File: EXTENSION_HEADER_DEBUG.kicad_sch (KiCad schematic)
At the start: 0 parts

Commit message: Weiter gemacht
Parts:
- added J8: Conn_01x16_MountingPin, Connector_PinHeader_2.54mm:PinHeader_2x08_P2.54mm_Vertical_SMD, symbol Connector_Generic_MountingPin:Conn_01x16_MountingPin
- added J9: Conn_01x04_MountingPin, Connector_PinHeader_2.54mm:PinHeader_1x04_P2.54mm_Vertical_SMD_Pin1Left, symbol Connector_Generic_MountingPin:Conn_01x04_MountingPin
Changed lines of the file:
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@@
 		(rev "Rev 1")
 	)
+	(symbol
+		(lib_id "Connector_Generic_MountingPin:Conn_01x04_MountingPin")
+		(at 66.04 154.94 0)
+		(unit 1)
+		(exclude_from_sim no)
+		(in_bom yes)
+		(on_board yes)
+		(dnp no)
+		(fields_autoplaced yes)
+		(property "Reference" "J9"
+			(at 68.58 155.2955 0)
+			(effects
+				(font
+					(size 1.27 1.27)
+				)
+				(justify left)
+			)
+		)
+		(property "Value" "Conn_01x04_MountingPin"
+			(at 68.58 157.8355 0)
+			(effects
+				(font
+					(size 1.27 1.27)
+				)
+				(justify left)
+			)
+		)
+		(property "Footprint" "Connector_PinHeader_2.54mm:PinHeader_1x04_P2.54mm_Vertical_SMD_Pin1Left"
+			(at 66.04 154.94 0)
+			(effects
+				(font
+					(size 1.27 1.27)
+				)
+				(hide yes)
+			)
+		)
+		(property "Datasheet" "~"
+			(at 66.04 154.94 0)
+			(effects
+				(font
+					(size 1.27 1.27)
+				)
+				(hide yes)
+			)
+		)
+		(property "Description" "Generic connectable mounting pin connector, single row, 01x04, script generated (kicad-library-utils/schlib/autogen/connector/)"
+			(at 66.04 154.94 0)
+			(effects
+				(font
+					(size 1.27 1.27)
+				)
+				(hide yes)
+			)
+		)
+		(pin "MP"
+		)
+		(pin "2"
+		)
+		(pin "3"
+		)
+		(pin "4"
+		)
+		(pin "1"
+		)
+		(instances
+			(project ""
+				(path "/96aa4cdc-6548-43b6-b96a-6d1618c17d83/727687ad-08f4-4d44-9d98-36b0cbf3889d"
+					(reference "J9")
+					(unit 1)
+				)
+			)
+		)
+	)
+	(symbol
+		(lib_id "Connector_Generic_MountingPin:Conn_01x16_MountingPin")
+		(at 67.31 106.68 0)
+		(unit 1)
+		(exclude_from_sim no)
+		(in_bom yes)
+		(on_board yes)
+		(dnp no)
+		(fields_autoplaced yes)
+		(property "Reference" "J8"
+			(at 69.85 107.0355 0)
+			(effects
+				(font
+					(size 1.27 1.27)
+				)
+				(justify left)
+			)
+		)
+		(property "Value" "Conn_01x16_MountingPin"
+			(at 69.85 109.5755 0)
+			(effects
+				(font
+					(size 1.27 1.27)
+				)
+				(justify left)
+			)
+		)
+		(property "Footprint" "Connector_PinHeader_2.54mm:PinHeader_2x08_P2.54mm_Vertical_SMD"
+			(at 67.31 106.68 0)
+			(effects
+				(font
+					(size 1.27 1.27)
+				)
+				(hide yes)
+			)
+		)
+		(property "Datasheet" "~"
+			(at 67.31 106.68 0)
+			(effects
+				(font
+					(size 1.27 1.27)
+				)
+				(hide yes)
+			)
+		)
+		(property "Description" "Generic connectable mounting pin connector, single row, 01x16, script generated (kicad-library-utils/schlib/autogen/connector/)"
+			(at 67.31 106.68 0)
+			(effects
+				(font
+					(size 1.27 1.27)
+				)
+				(hide yes)
+			)
+		)
+		(pin "6"
+		)
+		(pin "14"
+		)
+		(pin "4"
+		)
+		(pin "11"
+		)
+		(pin "1"
+		)
+		(pin "12"
+		)
+		(pin "10"
+		)
+		(pin "13"
+		)
+		(pin "MP"
+		)
+		(pin "2"
+		)
+		(pin "3"
+		)
+		(pin "5"
+		)
+		(pin "7"
+		)
+		(pin "8"
+		)
+		(pin "9"
+		)
+		(pin "15"
+		)
+		(pin "16"
+		)
+		(instances
+			(project ""
+				(path "/96aa4cdc-6548-43b6-b96a-6d1618c17d83/727687ad-08f4-4d44-9d98-36b0cbf3889d"
+					(reference "J8")
+					(unit 1)
+				)
+			)
+		)
+	)
 )

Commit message: Layout + Schematic weiter gemacht
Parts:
- removed J8: Conn_01x16_MountingPin, Connector_PinHeader_2.54mm:PinHeader_2x08_P2.54mm_Vertical_SMD, symbol Connector_Generic_MountingPin:Conn_01x16_MountingPin
- removed J9: Conn_01x04_MountingPin, Connector_PinHeader_2.54mm:PinHeader_1x04_P2.54mm_Vertical_SMD_Pin1Left, symbol Connector_Generic_MountingPin:Conn_01x04_MountingPin
- added H1, H2, H3, H4: MountingHole_Pad_MP, MountingHole:MountingHole_3.2mm_M3_Pad, symbol Mechanical:MountingHole_Pad_MP
- added J8: Conn_01x16_Pin, Connector_PinHeader_2.54mm:PinHeader_2x08_P2.54mm_Vertical_SMD, symbol Connector:Conn_01x16_Pin
- added J9: Conn_01x04_Pin, Connector_PinHeader_2.54mm:PinHeader_1x04_P2.54mm_Vertical_SMD_Pin1Left, symbol Connector:Conn_01x04_Pin
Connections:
- new net GND: H1.MP, H2.MP, H3.MP, H4.MP

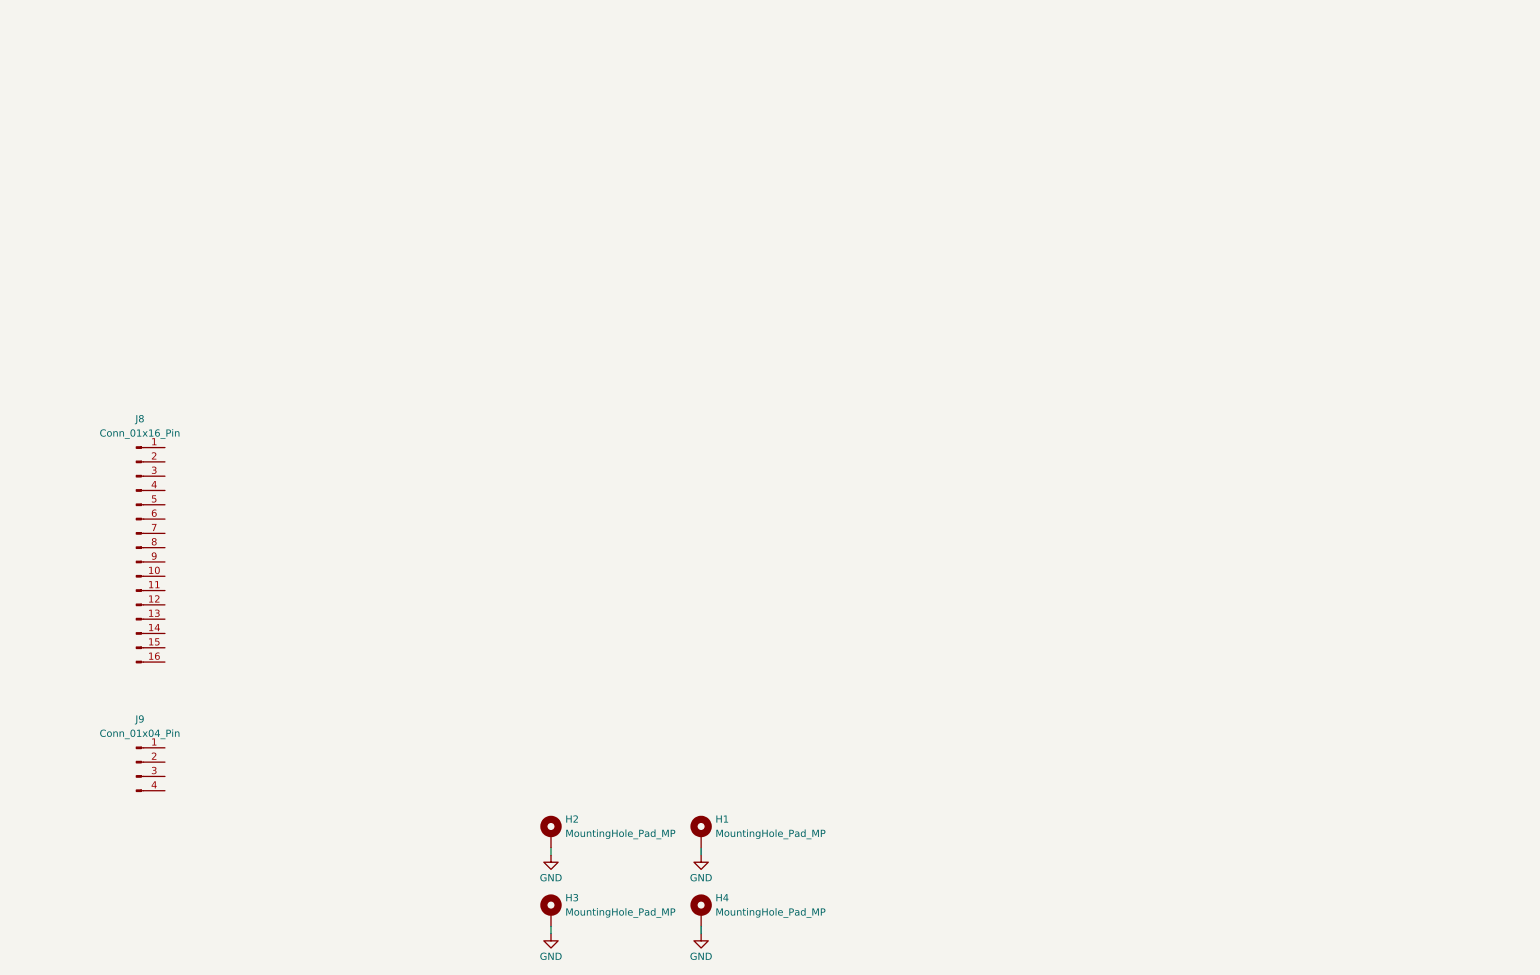
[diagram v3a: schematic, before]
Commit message: Button & Power Sequencing + Layout
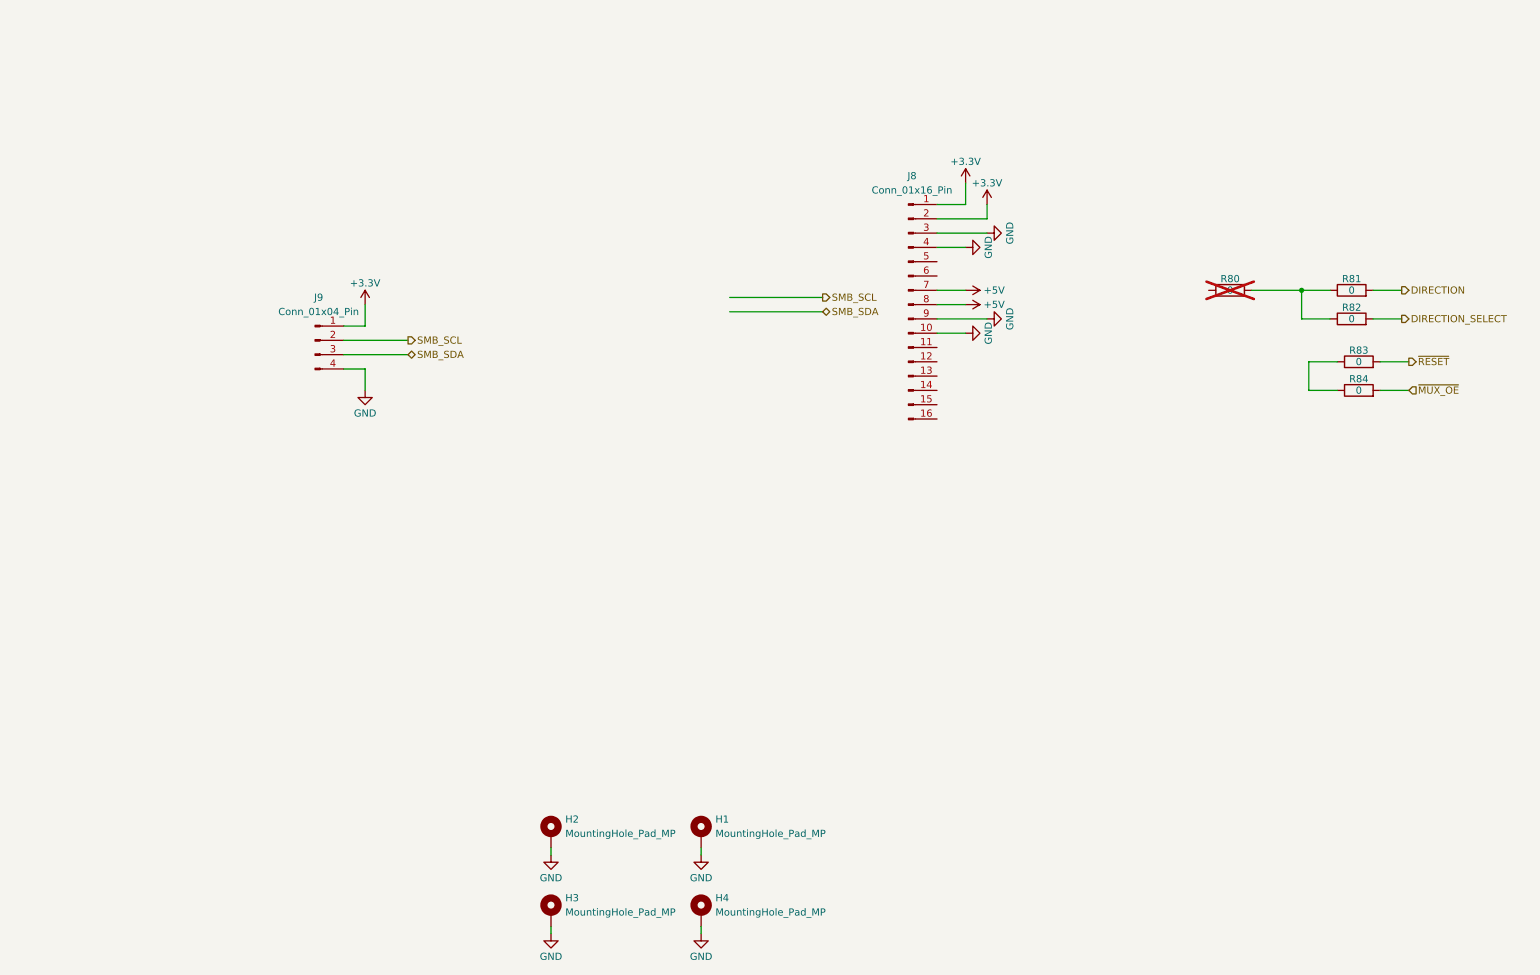
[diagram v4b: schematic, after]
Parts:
- added R80, R81, R82, R83, R84: 0, 00_Resistor:Res_0402, symbol Device:R
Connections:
- net GND: now also J8.10 (Pin_10), J8.3 (Pin_3), J8.4 (Pin_4), J8.9 (Pin_9), J9.4 (Pin_4)
- net +3.3V: now reaches J9.1 (Pin_1)
- net +3.3V: now also J8.1 (Pin_1), J8.2 (Pin_2)
- net SMB_SCL: now reaches J9.2 (Pin_2)
- net SMB_SDA: now reaches J9.3 (Pin_3)
- net +5V: now reaches J8.7 (Pin_7)
- net +5V: now also J8.8 (Pin_8)
- new net: R83.1, R84.1
- new net: R80.2, R81.1, R82.1
- new net DIRECTION: R81.2
- new net DIRECTION_SELECT: R82.2
- new net ~{MUX_OE}: R84.2
- new net ~{RESET}: R83.2
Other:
- moved on the sheet: J8, J9

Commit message: Diff Pair neu, Layout fast fertig
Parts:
- removed H1, H2, H3, H4: MountingHole_Pad_MP, MountingHole:MountingHole_3.2mm_M3_Pad, symbol Mechanical:MountingHole_Pad_MP
- removed R82, R83, R84: 0, 00_Resistor:Res_0402, symbol Device:R
- added C119, C120, C127, C128: 100n, 00_Capacitor:Cap_0402, symbol Device:C
- added C121, C122, C123, C124, C125, C126: 10u, 00_Capacitor:Cap_0603, symbol Device:C
- added H1, H2, H3, H4: MountingHole_Pad, MountingHole:MountingHole_3.2mm_M3_Pad_TopBottom, symbol Mechanical:MountingHole_Pad
- added Q4, Q5: NTJD4401NT1G, Package_TO_SOT_SMD:SOT-363_SC-70-6, symbol ANR_Blastec_Lib:NTJD4401NT1G
- added R85, R86, R87, R88, R89, R90, R91, R92: 10k, 00_Resistor:Res_0402, symbol Device:R
- added U26: 74LVC1G32, Package_TO_SOT_SMD:SOT-23-5, symbol 74xGxx:74LVC1G32
- added U27: 74LVC1G08, Package_TO_SOT_SMD:SOT-23-5, symbol 74xGxx:74LVC1G08
- added U28: ISO1540, Package_SO:SOIC-8_3.9x4.9mm_P1.27mm, symbol Isolator:ISO1540
- R80: footprint 00_Resistor:Res_0402 -> 00_Resistor:Res_0603
- R81: footprint 00_Resistor:Res_0402 -> 00_Resistor:Res_0603; now not fitted
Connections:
- net +3.3V: now also R80.2, R81.2, C119.1, C120.1, C123.1, C124.1, C125.1, C127.1, R86.1, R91.1, R92.1, U26.5 (VCC), U27.5 (VCC), U28.8 (VCC2); no longer J8.1 (Pin_1), J8.2 (Pin_2)
- net +5V: now also C121.1, C122.1
- net DIRECTION: now also U26.1; no longer R81.2
- net DIRECTION_SELECT: now also R85.1, U26.4
- net GND: now also J8.16 (Pin_16), C119.2, C120.2, C121.2, C122.2, C123.2, C124.2, C125.2, C126.2, C127.2, C128.2, H1.1, H2.1, H3.1, H4.1, Q4.1 (S), Q4.4 (S), Q5.1 (S), Q5.4 (S), R85.2, R87.2, R89.2, R90.2, U26.3 (GND), U27.3 (GND), U28.4 (GND1), U28.5 (GND2)
- net SMB_SCL: now also U28.6 (SCL2)
- net SMB_SDA: now also U28.7 (SDA2)
- net ~{MUX_OE}: now also R89.1, U27.4
- net ~{RESET}: now also Q5.2 (G), U27.1
- net at R81.1: now also J8.2 (Pin_2); no longer R80.2
- net at R80.1: now also J8.1 (Pin_1)
- net at J8.11 (Pin_11): now also Q5.3 (D), R88.2
- net VCC_EXT: now reaches J8.12 (Pin_12)
- net VCC_EXT: now also C126.1, C128.1, R88.1, U28.1 (VCC1)
- net DIRECTION_EXT: now reaches J8.13 (Pin_13)
- net DIRECTION_EXT: now also Q4.2 (G), R87.1
- net ~{MUX_OE_EXT}: now reaches J8.14 (Pin_14)
- net ~{MUX_OE_EXT}: now also Q4.5 (G), R90.1
- net I2C_SDA_EXT: now reaches J8.5 (Pin_5)
- net I2C_SDA_EXT: now also U28.2 (SDA1)
- net I2C_SCL_EXT: now reaches J8.6 (Pin_6)
- net I2C_SCL_EXT: now also U28.3 (SCL1)
- new net: Q4.3 (D), R91.2, U27.2
- new net: Q4.6 (D), R86.2, U26.2
- new net: Q5.5 (G), Q5.6 (D), R92.2
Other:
- moved on the sheet: J8, J9

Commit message: Powersequencing
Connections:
- no-connect marks 0 -> 1
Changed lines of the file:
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@@
 		(color 0 0 0 0)
+	)
+	(no_connect
+		(at 100.33 100.33)
 	)
 	(wire

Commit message: Schaltplan erweitert, Kleinzeug
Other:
- moved on the sheet: C126, C127, C128
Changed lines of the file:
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@@
 	(wire
 		(pts
-			(xy 48.26 59.69) (xy 48.26 60.96)
+			(xy 35.56 58.42) (xy 35.56 59.69)
 		)
 		(stroke
@@
 	(wire
 		(pts
-			(xy 185.42 119.38) (xy 190.5 119.38)
+			(xy 181.61 119.38) (xy 190.5 119.38)
 		)
 		(stroke
@@
 	(wire
 		(pts
-			(xy 58.42 68.58) (xy 58.42 72.39)
+			(xy 45.72 67.31) (xy 45.72 68.58)
 		)
 		(stroke
@@
 	(wire
 		(pts
-			(xy 35.56 59.69) (xy 35.56 60.96)
+			(xy 72.39 58.42) (xy 72.39 59.69)
 		)
 		(stroke
@@
 	(wire
 		(pts
-			(xy 35.56 69.85) (xy 35.56 68.58)
+			(xy 72.39 68.58) (xy 72.39 67.31)
 		)
 		(stroke
@@
 	(wire
 		(pts
-			(xy 48.26 69.85) (xy 48.26 68.58)
+			(xy 35.56 68.58) (xy 35.56 67.31)
 		)
 		(stroke
@@
 	(wire
 		(pts
-			(xy 58.42 57.15) (xy 58.42 60.96)
+			(xy 45.72 58.42) (xy 45.72 59.69)
 		)
 		(stroke
@@
 	(hierarchical_label "~{RESET}"
 		(shape input)
-		(at 185.42 119.38 180)
+		(at 181.61 119.38 180)
 		(effects
 			(font
@@
 	(symbol
 		(lib_id "power:GND")
-		(at 35.56 69.85 0)
+		(at 72.39 68.58 0)
 		(unit 1)
 		(body_style 1)
@@
 		(dnp no)
 		(property "Reference" "#PWR0292"
-			(at 35.56 76.2 0)
+			(at 72.39 74.93 0)
 			(hide yes)
 			(show_name no)
@@
 		)
 		(property "Value" "GND"
-			(at 35.56 73.914 0)
+			(at 72.39 72.644 0)
 			(show_name no)
 			(do_not_autoplace no)
@@
 		)
 		(property "Footprint" ""
-			(at 35.56 69.85 0)
+			(at 72.39 68.58 0)
 			(hide yes)
 			(show_name no)
@@
 		)
 		(property "Datasheet" ""
-			(at 35.56 69.85 0)
+			(at 72.39 68.58 0)
 			(hide yes)
 			(show_name no)
@@
 		)
 		(property "Description" "Power symbol creates a global label with name \"GND\" , ground"
-			(at 35.56 69.85 0)
+			(at 72.39 68.58 0)
 			(hide yes)
 			(show_name no)
@@
 	(symbol
 		(lib_id "power:GND")
-		(at 58.42 72.39 0)
+		(at 45.72 68.58 0)
 		(unit 1)
 		(body_style 1)
@@
 		(dnp no)
 		(property "Reference" "#PWR0284"
-			(at 58.42 78.74 0)
+			(at 45.72 74.93 0)
 			(hide yes)
 			(show_name no)
@@
 		)
 		(property "Value" "GND"
-			(at 58.42 76.454 0)
+			(at 45.72 72.644 0)
 			(show_name no)
 			(do_not_autoplace no)
@@
 		)
 		(property "Footprint" ""
-			(at 58.42 72.39 0)
+			(at 45.72 68.58 0)
 			(hide yes)
 			(show_name no)
@@
 		)
 		(property "Datasheet" ""
-			(at 58.42 72.39 0)
+			(at 45.72 68.58 0)
 			(hide yes)
 			(show_name no)
@@
 		)
 		(property "Description" "Power symbol creates a global label with name \"GND\" , ground"
-			(at 58.42 72.39 0)
+			(at 45.72 68.58 0)
 			(hide yes)
 			(show_name no)
@@
 	(symbol
 		(lib_id "Device:C")
-		(at 48.26 64.77 0)
+		(at 35.56 63.5 0)
 		(mirror y)
 		(unit 1)
@@
 		(dnp no)
 		(property "Reference" "C128"
-			(at 44.45 63.4999 0)
+			(at 31.75 62.2299 0)
 			(show_name no)
 			(do_not_autoplace no)
@@
 		)
 		(property "Value" "100n"
-			(at 44.45 66.0399 0)
+			(at 31.75 64.7699 0)
 			(show_name no)
 			(do_not_autoplace no)
@@
 		)
 		(property "Footprint" "00_Capacitor:Cap_0402"
-			(at 47.2948 68.58 0)
+			(at 34.5948 67.31 0)
 			(hide yes)
 			(show_name no)
@@
 		)
 		(property "Datasheet" ""
-			(at 48.26 64.77 0)
+			(at 35.56 63.5 0)
 			(hide yes)
 			(show_name no)
@@
 		)
 		(property "Description" "Unpolarized capacitor"
-			(at 48.26 64.77 0)
+			(at 35.56 63.5 0)
 			(hide yes)
 			(show_name no)
@@
 	(symbol
 		(lib_id "power:GND")
-		(at 48.26 69.85 0)
+		(at 35.56 68.58 0)
 		(unit 1)
 		(body_style 1)
@@
 		(dnp no)
 		(property "Reference" "#PWR0294"
-			(at 48.26 76.2 0)
+			(at 35.56 74.93 0)
 			(hide yes)
 			(show_name no)
@@
 		)
 		(property "Value" "GND"
-			(at 48.26 73.914 0)
+			(at 35.56 72.644 0)
 			(show_name no)
 			(do_not_autoplace no)
@@
 		)
 		(property "Footprint" ""
-			(at 48.26 69.85 0)
+			(at 35.56 68.58 0)
 			(hide yes)
 			(show_name no)
@@
 		)
 		(property "Datasheet" ""
-			(at 48.26 69.85 0)
+			(at 35.56 68.58 0)
 			(hide yes)
 			(show_name no)
@@
 		)
 		(property "Description" "Power symbol creates a global label with name \"GND\" , ground"
-			(at 48.26 69.85 0)
+			(at 35.56 68.58 0)
 			(hide yes)
 			(show_name no)
@@
 	(symbol
 		(lib_id "Device:C")
-		(at 58.42 64.77 0)
+		(at 45.72 63.5 0)
 		(unit 1)
 		(body_style 1)
@@
 		(fields_autoplaced yes)
 		(property "Reference" "C126"
-			(at 62.23 63.4999 0)
+			(at 49.53 62.2299 0)
 			(show_name no)
 			(do_not_autoplace no)
@@
 		)
 		(property "Value" "10u"
-			(at 62.23 66.0399 0)
+			(at 49.53 64.7699 0)
 			(show_name no)
 			(do_not_autoplace no)
@@
 		)
 		(property "Footprint" "00_Capacitor:Cap_0603"
-			(at 59.3852 68.58 0)
+			(at 46.6852 67.31 0)
 			(hide yes)
 			(show_name no)
@@
 		)
 		(property "Datasheet" ""
-			(at 58.42 64.77 0)
+			(at 45.72 63.5 0)
 			(hide yes)
 			(show_name no)
@@
 		)
 		(property "Description" "Unpolarized capacitor"
-			(at 58.42 64.77 0)
+			(at 45.72 63.5 0)
 			(hide yes)
 			(show_name no)
@@
 	(symbol
 		(lib_id "power:VCC")
-		(at 58.42 57.15 0)
+		(at 45.72 58.42 0)
 		(unit 1)
 		(body_style 1)
@@
 		(dnp no)
 		(property "Reference" "#PWR0283"
-			(at 58.42 60.96 0)
+			(at 45.72 62.23 0)
 			(hide yes)
 			(show_name no)
@@
 		)
 		(property "Value" "VCC_EXT"
-			(at 58.42 53.086 0)
+			(at 45.72 54.356 0)
 			(show_name no)
 			(do_not_autoplace no)
@@
 		)
 		(property "Footprint" ""
-			(at 58.42 57.15 0)
+			(at 45.72 58.42 0)
 			(hide yes)
 			(show_name no)
@@
 		)
 		(property "Datasheet" ""
-			(at 58.42 57.15 0)
+			(at 45.72 58.42 0)
 			(hide yes)
 			(show_name no)
@@
 		)
 		(property "Description" "Power symbol creates a global label with name \"VCC\""
-			(at 58.42 57.15 0)
+			(at 45.72 58.42 0)
 			(hide yes)
 			(show_name no)
@@
 	(symbol
 		(lib_id "power:+3.3V")
-		(at 35.56 59.69 0)
+		(at 72.39 58.42 0)
 		(unit 1)
 		(body_style 1)
@@
 		(dnp no)
 		(property "Reference" "#PWR0291"
-			(at 35.56 63.5 0)
+			(at 72.39 62.23 0)
 			(hide yes)
 			(show_name no)
@@
 		)
 		(property "Value" "+3.3V"
-			(at 35.56 55.88 0)
+			(at 72.39 54.61 0)
 			(show_name no)
 			(do_not_autoplace no)
@@
 		)
 		(property "Footprint" ""
-			(at 35.56 59.69 0)
+			(at 72.39 58.42 0)
 			(hide yes)
 			(show_name no)
@@
 		)
 		(property "Datasheet" ""
-			(at 35.56 59.69 0)
+			(at 72.39 58.42 0)
 			(hide yes)
 			(show_name no)
@@
 		)
 		(property "Description" "Power symbol creates a global label with name \"+3.3V\""
-			(at 35.56 59.69 0)
+			(at 72.39 58.42 0)
 			(hide yes)
 			(show_name no)
@@
 	(symbol
 		(lib_id "Device:C")
-		(at 35.56 64.77 0)
+		(at 72.39 63.5 0)
 		(mirror y)
 		(unit 1)
@@
 		(dnp no)
 		(property "Reference" "C127"
-			(at 31.75 63.4999 0)
+			(at 68.58 62.2299 0)
 			(show_name no)
 			(do_not_autoplace no)
@@
 		)
 		(property "Value" "100n"
-			(at 31.75 66.0399 0)
+			(at 68.58 64.7699 0)
 			(show_name no)
 			(do_not_autoplace no)
@@
 		)
 		(property "Footprint" "00_Capacitor:Cap_0402"
-			(at 34.5948 68.58 0)
+			(at 71.4248 67.31 0)
 			(hide yes)
 			(show_name no)
@@
 		)
 		(property "Datasheet" ""
-			(at 35.56 64.77 0)
+			(at 72.39 63.5 0)
 			(hide yes)
 			(show_name no)
@@
 		)
 		(property "Description" "Unpolarized capacitor"
-			(at 35.56 64.77 0)
+			(at 72.39 63.5 0)
 			(hide yes)
 			(show_name no)
@@
 	(symbol
 		(lib_id "power:VCC")
-		(at 48.26 59.69 0)
+		(at 35.56 58.42 0)
 		(unit 1)
 		(body_style 1)
@@
 		(dnp no)
 		(property "Reference" "#PWR0293"
-			(at 48.26 63.5 0)
+			(at 35.56 62.23 0)
 			(hide yes)
 			(show_name no)
@@
 		)
 		(property "Value" "VCC_EXT"
-			(at 48.26 55.626 0)
+			(at 35.56 54.356 0)
 			(show_name no)
 			(do_not_autoplace no)
@@
 		)
 		(property "Footprint" ""
-			(at 48.26 59.69 0)
+			(at 35.56 58.42 0)
 			(hide yes)
 			(show_name no)
@@
 		)
 		(property "Datasheet" ""
-			(at 48.26 59.69 0)
+			(at 35.56 58.42 0)
 			(hide yes)
 			(show_name no)
@@
 		)
 		(property "Description" "Power symbol creates a global label with name \"VCC\""
-			(at 48.26 59.69 0)
+			(at 35.56 58.42 0)
 			(hide yes)
 			(show_name no)
